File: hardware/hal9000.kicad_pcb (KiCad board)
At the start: 2 copper layers, 53.6 x 59.9 mm, 17 parts

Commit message: hw: reva2 kicad files
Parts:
- C2: footprint Capacitor_SMD:C_0805_2012Metric_Pad1.18x1.45mm_HandSolder -> Capacitor_THT:CP_Radial_D6.3mm_P2.50mm
- moved J_PHOTON_R1 28.1 mm to (160.6, 86.9), turned to 0 degrees
- moved C2 8.51 mm to (136.7, 86.8)
- moved ? 4.43 mm to (175.5, 120.9)
- moved ? 4.35 mm to (175.5, 67.0)
- moved J_BUTTON1 3.46 mm to (168.7, 104.6)
- moved ? 2.73 mm to (121.7, 120.9)
- moved J_LED1 2.59 mm to (168.7, 114.8)
- moved R1 2.59 mm to (164.9, 114.8)
- moved ? 2.59 mm to (121.7, 67.0)
- moved J_BATT1 1.97 mm to (130.2, 68.8), turned to 90 degrees
- moved J_AMP1 1.78 mm to (130.3, 109.7)
- moved J_BUCK1 1.78 mm to (130.2, 86.8)
- moved J_MIC1 1.78 mm to (130.2, 96.8)
- moved J_SW1 1.78 mm to (130.2, 76.8)
- moved C1 1.53 mm to (137.1, 102.4)
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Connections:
- J_BUTTON1 pad 1: Net-(J_BUTTON1-Pin_1) -> /D3
- J_PHOTON_R1 pad 1: Net-(J_PHOTON_R1-Pin_1) -> +3V3
- J_PHOTON_R1 pad 12: +3V3 -> /D0
- J_PHOTON_R1 pad 4: Net-(J_BUTTON1-Pin_1) -> unconnected-(J_PHOTON_R1-Pin_4-Pad4)
- J_PHOTON_R1 pad 8: unconnected-(J_PHOTON_R1-Pin_8-Pad8) -> /D3
- R1 pad 2: Net-(J_PHOTON_R1-Pin_1) -> /D0
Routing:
- net /D3: track 0.00 -> 8.18 mm
- net Net-(J_BUTTON1-Pin_1): track 8.03 -> 0.00 mm
- net Net-(J_PHOTON_R1-Pin_1): track 4.04 -> 0.00 mm
- net /D0: track 0.00 -> 3.73 mm
- net GND: track 9.63 -> 6.47 mm
- net +3V3: track 68.5 -> 71.6 mm
- net /A6: track 6.37 -> 8.28 mm
- net /A3: track 13.0 -> 14.7 mm
- net +5V: track 43.3 -> 41.8 mm
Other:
- board size 53.6 x 59.9 mm -> 59.9 x 59.9 mm
- board text added: "PWR SWITCH"
- board text added: "REV A2"
- board text removed: "SWITCH"

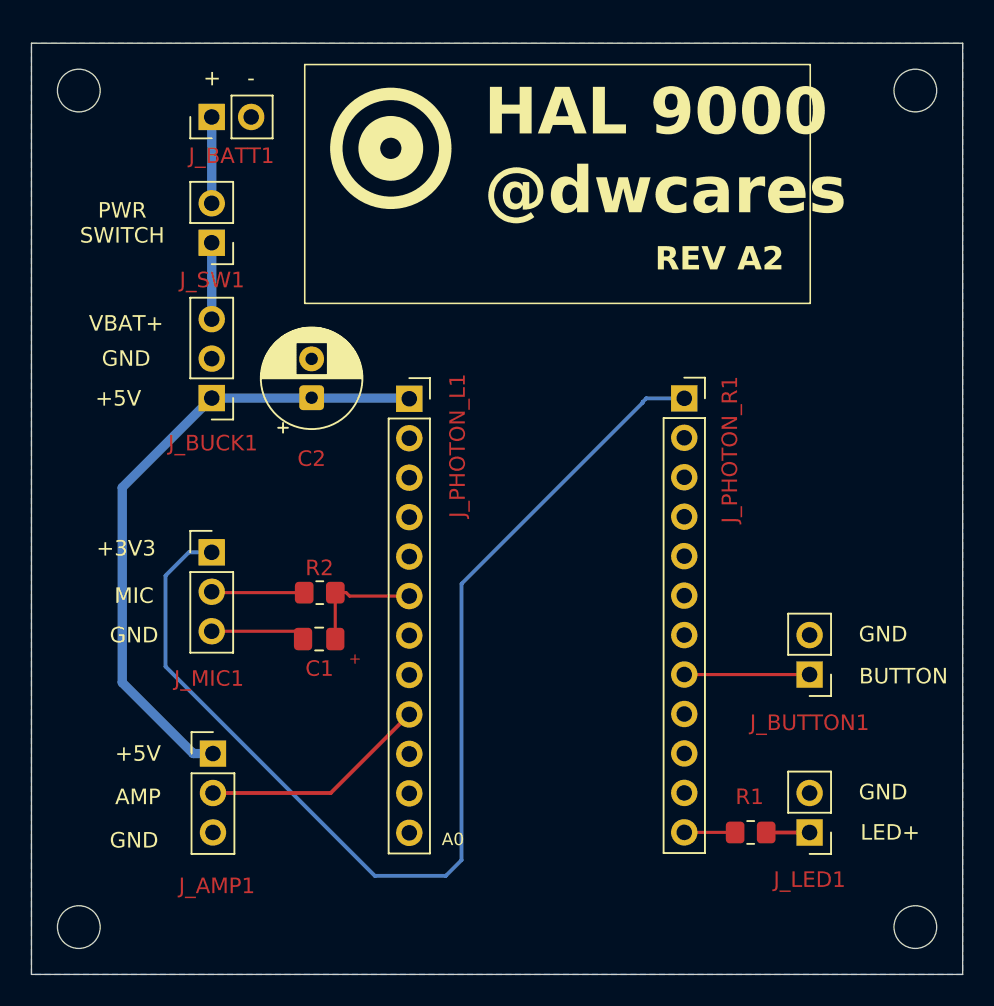
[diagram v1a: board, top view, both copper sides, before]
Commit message: Update hw/fw to match reva2 and reva3 pushbutton at D4
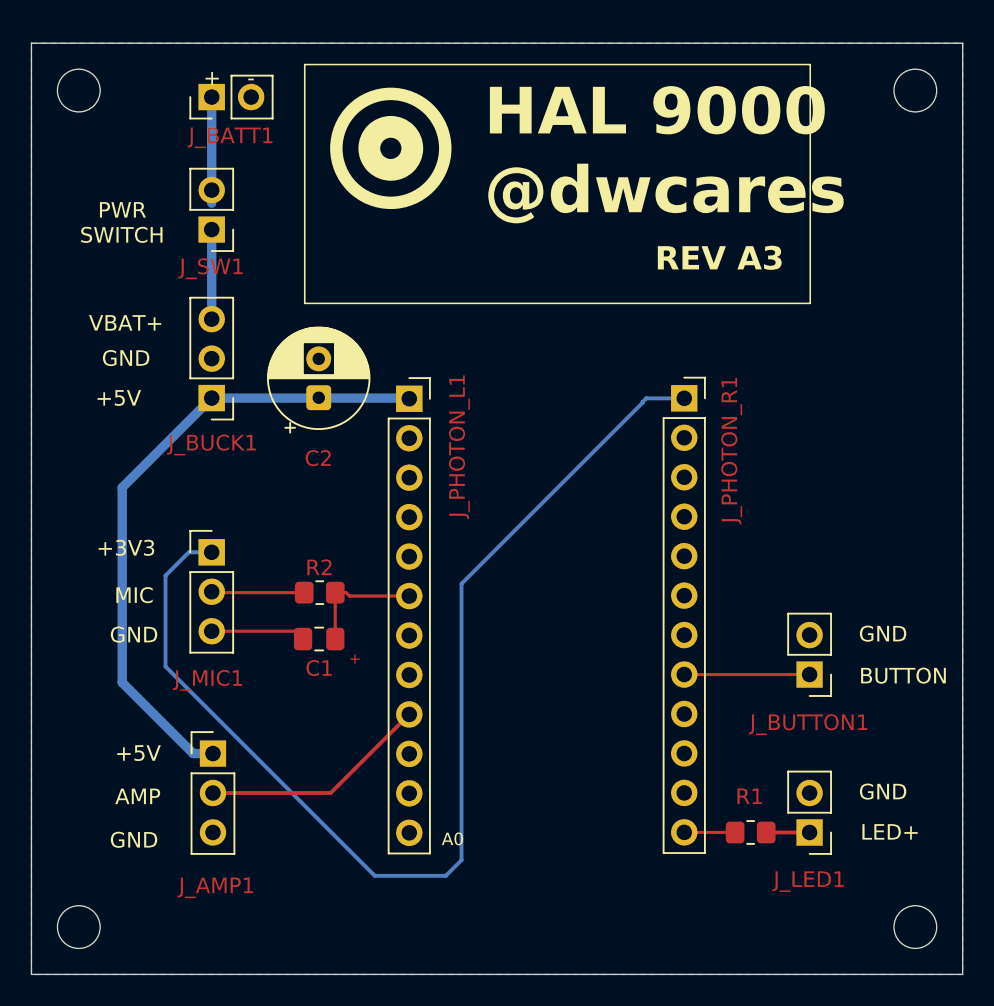
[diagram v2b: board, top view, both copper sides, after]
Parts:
- moved J_BATT1 1.28 mm to (130.2, 67.5)
- moved J_SW1 0.85 mm to (130.2, 76.0)
- moved C2 0.46 mm to (137.1, 86.8)
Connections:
- net /D3 renamed /D4
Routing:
- net Net-(J_BATT1-Pin_1): track 4.71 -> 6.84 mm
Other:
- board text added: "REV A3"
- board text removed: "REV A2"
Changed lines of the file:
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@@
 	(net 25 "unconnected-(J_PHOTON_R1-Pin_10-Pad10)")
 	(net 26 "unconnected-(J_PHOTON_R1-Pin_9-Pad9)")
-	(net 27 "/D3")
+	(net 27 "/D4")
 	(net 28 "/D0")
 	(footprint "Connector_PinHeader_2.54mm:PinHeader_1x03_P2.54mm_Vertical"
@@
 			(layers "*.Cu" "*.Mask")
 			(remove_unused_layers no)
-			(net 27 "/D3")
+			(net 27 "/D4")
 			(pinfunction "Pin_1")
 			(pintype "passive")
@@
 			(layers "*.Cu" "*.Mask")
 			(remove_unused_layers no)
-			(net 27 "/D3")
+			(net 27 "/D4")
 			(pinfunction "Pin_8")
 			(pintype "passive")
@@
 	(footprint "Connector_PinHeader_2.54mm:PinHeader_1x02_P2.54mm_Vertical"
 		(layer "F.Cu")
-		(at 130.222 68.75 90)
+		(at 130.222 67.47 90)
 		(descr "Through hole straight pin header, 1x02, 2.54mm pitch, single row")
 		(tags "Through hole pin header THT 1x02 2.54mm single row")
@@
 	(footprint "Capacitor_THT:CP_Radial_D6.3mm_P2.50mm"
 		(layer "F.Cu")
-		(at 136.652 86.822 90)
+		(at 137.11 86.822 90)
 		(descr "CP, Radial series, Radial, pin pitch=2.50mm, diameter=6.3mm, height=7mm, Electrolytic Capacitor")
 		(tags "CP Radial series Radial pin pitch 2.50mm diameter 6.3mm height 7mm Electrolytic Capacitor")
@@
 	(footprint "Connector_PinHeader_2.54mm:PinHeader_1x02_P2.54mm_Vertical"
 		(layer "F.Cu")
-		(at 130.222 76.846 180)
+		(at 130.222 76 180)
 		(descr "Through hole straight pin header, 1x02, 2.54mm pitch, single row")
 		(tags "Through hole pin header THT 1x02 2.54mm single row")
@@
 		)
 	)
-	(gr_text "REV A2"
+	(gr_text "REV A3"
 		(at 158.75 78.75 0)
 		(layer "F.SilkS")
@@
 			(justify left bottom)
 		)
-		(render_cache "REV A2" 0
+		(render_cache "REV A3" 0
 			(polygon
 				(pts
@@
 			(polygon
 				(pts
-					(xy 164.648739 78.495) (xy 164.648739 78.312459) (xy 164.965369 77.994637) (xy 165.108251 77.841131)
-					(xy 165.157899 77.777392) (xy 165.191325 77.726001) (xy 165.216239 77.675525) (xy 165.229701 77.632395)
-					(xy 165.238952 77.543368) (xy 165.235855 77.506357) (xy 165.226679 77.471469) (xy 165.211444 77.439418)
-					(xy 165.190775 77.412393) (xy 165.164594 77.390254) (xy 165.131332 77.372643) (xy 165.093829 77.361678)
-					(xy 165.049358 77.357805) (xy 164.972993 77.366669) (xy 164.902813 77.392976) (xy 164.8378 77.433381)
-					(xy 164.774768 77.486765) (xy 164.642602 77.315032) (xy 164.735181 77.241497) (xy 164.83879 77.18424)
-					(xy 164.912946 77.15709) (xy 164.991392 77.140644) (xy 165.075004 77.135055) (xy 165.170564 77.141585)
-					(xy 165.253332 77.160151) (xy 165.328429 77.191695) (xy 165.390169 77.23434) (xy 165.440291 77.289114)
-					(xy 165.478279 77.357164) (xy 165.501338 77.434473) (xy 165.509512 77.526974) (xy 165.504003 77.604975)
-					(xy 165.487988 77.675901) (xy 165.461837 77.743528) (xy 165.425431 77.810448) (xy 165.380631 77.874761)
-					(xy 165.324498 77.941423) (xy 165.187752 78.079542) (xy 164.99303 78.266388) (xy 165.557689 78.266388)
-					(xy 165.557689 78.495)
+					(xy 165.561719 78.088885) (xy 165.5522 78.184759) (xy 165.524808 78.267854) (xy 165.478641 78.340726)
+					(xy 165.411601 78.403134) (xy 165.328292 78.451186) (xy 165.219443 78.488771) (xy 165.098285 78.510489)
+					(xy 164.94696 78.518447) (xy 164.873595 78.516707) (xy 164.7973 78.512035) (xy 164.723477 78.504983)
+					(xy 164.658997 78.495) (xy 164.658997 78.278112) (xy 164.803986 78.299269) (xy 164.971506 78.307421)
+					(xy 165.053582 78.303585) (xy 165.118052 78.293224) (xy 165.17589 78.275124) (xy 165.219443 78.2521)
+					(xy 165.254548 78.221621) (xy 165.278428 78.185605) (xy 165.292501 78.144109) (xy 165.297387 78.096212)
+					(xy 165.292419 78.053917) (xy 165.277878 78.016436) (xy 165.253853 77.983885) (xy 165.218435 77.95562)
+					(xy 165.174956 77.934122) (xy 165.116495 77.916785) (xy 165.051635 77.906686) (xy 164.969491 77.902955)
+					(xy 164.82093 77.902955) (xy 164.82093 77.709515) (xy 164.957218 77.709515) (xy 165.033555 77.705154)
+					(xy 165.089842 77.693669) (xy 165.138903 77.674346) (xy 165.173922 77.651354) (xy 165.200836 77.622149)
+					(xy 165.218435 77.588614) (xy 165.22844 77.55159) (xy 165.231808 77.512502) (xy 165.225401 77.460588)
+					(xy 165.207531 77.420169) (xy 165.178502 77.388488) (xy 165.140522 77.366534) (xy 165.087166 77.351704)
+					(xy 165.013546 77.346081) (xy 164.934125 77.350092) (xy 164.855735 77.36211) (xy 164.694901 77.404699)
+					(xy 164.694901 77.193674) (xy 164.783012 77.167021) (xy 164.867001 77.148977) (xy 164.952089 77.138261)
+					(xy 165.041207 77.135055) (xy 165.148132 77.141342) (xy 165.23538 77.158686) (xy 165.313938 77.188052)
+					(xy 165.375789 77.225822) (xy 165.425821 77.274439) (xy 165.461335 77.332068) (xy 165.482638 77.397261)
+					(xy 165.490003 77.471561) (xy 165.483172 77.551233) (xy 165.464137 77.616079) (xy 165.434132 77.669031)
+					(xy 165.392914 77.714476) (xy 165.341356 77.75291) (xy 165.277878 77.784436) (xy 165.340233 77.798669)
+					(xy 165.394657 77.81979) (xy 165.443577 77.848736) (xy 165.484324 77.884362) (xy 165.517372 77.926729)
+					(xy 165.541752 77.975129) (xy 165.556566 78.028257)
 				)
 			)
@@
 	(segment
 		(start 130.222 74.306)
-		(end 130.222 69.596)
+		(end 130.222 67.47)
 		(width 0.6)
 		(layer "B.Cu")
